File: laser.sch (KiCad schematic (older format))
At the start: 0 parts

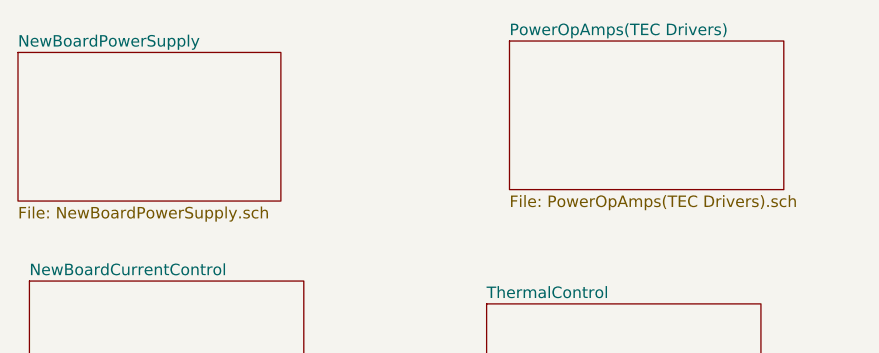
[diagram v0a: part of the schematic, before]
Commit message: added 4.2V port from pwr supply to pwr op amps sheet
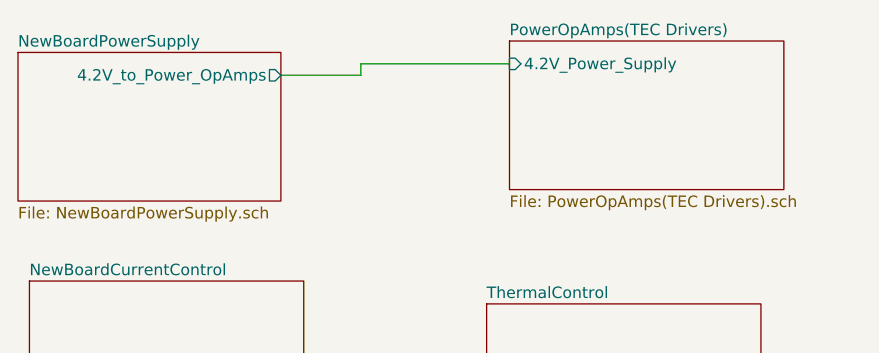
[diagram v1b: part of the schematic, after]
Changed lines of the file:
@@
 F0 "NewBoardPowerSupply" 50
 F1 "NewBoardPowerSupply.sch" 50
+F2 "4.2V_to_Power_OpAmps" O R 2850 1350 50
 $EndSheet
 $Sheet
@@
 F0 "PowerOpAmps(TEC Drivers)" 50
 F1 "PowerOpAmps(TEC Drivers).sch" 50
+F2 "4.2V_Power_Supply" I L 3850 1300 50
 $EndSheet
 $Sheet
@@
 F1 "ArduinoNano.sch" 50
 $EndSheet
+Wire Wire Line
+	2850 1350 3200 1350
+Wire Wire Line
+	3200 1350 3200 1300
+Wire Wire Line
+	3200 1300 3850 1300
 $EndSCHEMATC

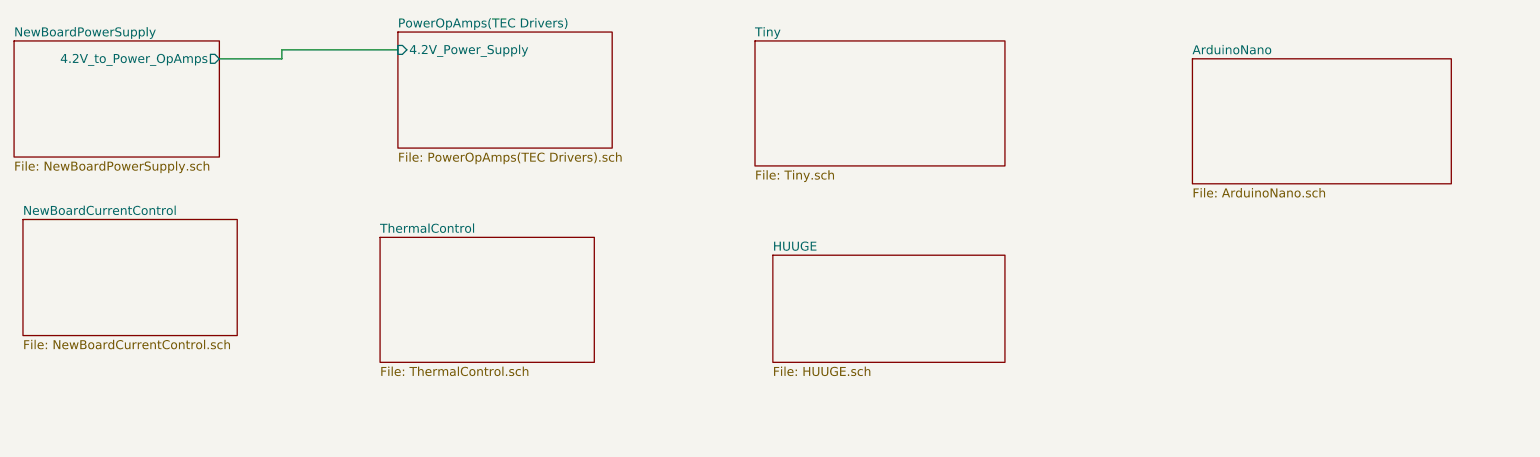
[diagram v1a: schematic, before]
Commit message: added 5v power source 'ports'
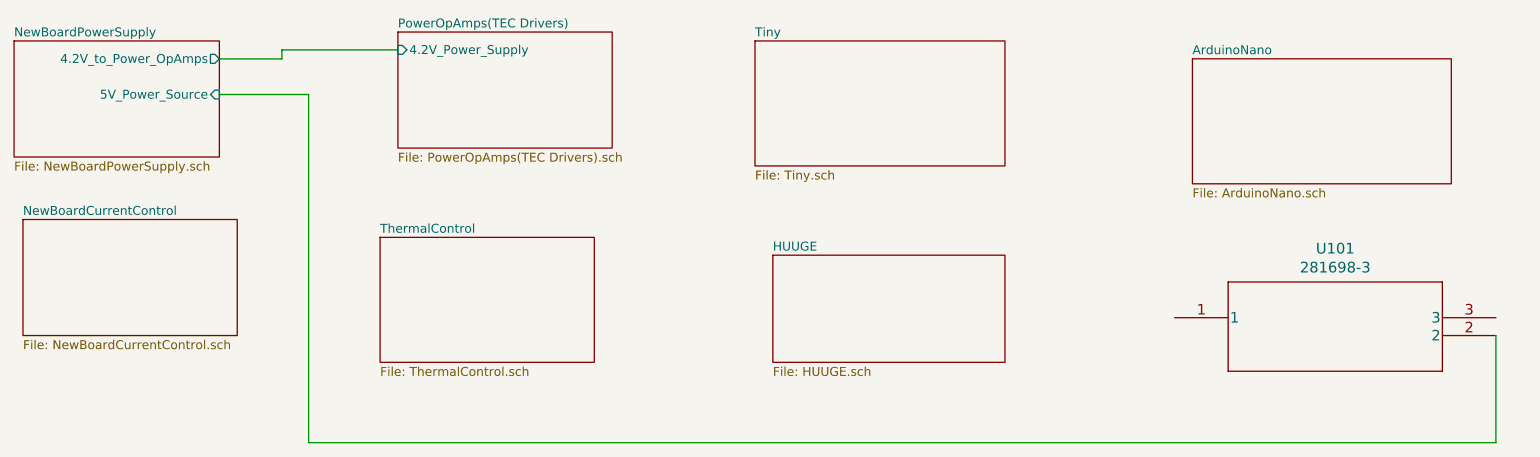
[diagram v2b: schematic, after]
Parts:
- added U101: 281698-3, footprint libraries:281698-3, symbol 3PinHeader:281698-3
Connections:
- new net NewBoardPowerSupply/5V_Power_Source: U101.2
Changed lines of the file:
@@
 F1 "NewBoardPowerSupply.sch" 50
 F2 "4.2V_to_Power_OpAmps" O R 2850 1350 50
+F3 "5V_Power_Source" I R 2850 1550 50
 $EndSheet
 $Sheet
@@
 Wire Wire Line
 	3200 1300 3850 1300
+$Comp
+L 3PinHeader:281698-3 U101
+U 1 1 60DB4391
+P 8200 2800
+F 0 "U101" H 9100 3187 60  0000 C CNN
+F 1 "281698-3" H 9100 3081 60  0000 C CNN
+F 2 "footprint libraries:281698-3" H 9100 3040 60  0001 C CNN
+F 3 "" H 8200 2800 60  0000 C CNN
+	1    8200 2800
+	1    0    0    -1
+$EndComp
+Wire Wire Line
+	2850 1550 3350 1550
+Wire Wire Line
+	3350 1550 3350 3500
+Wire Wire Line
+	3350 3500 10000 3500
+Wire Wire Line
+	10000 3500 10000 2900
 $EndSCHEMATC

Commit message: connect 5V label from nano on main
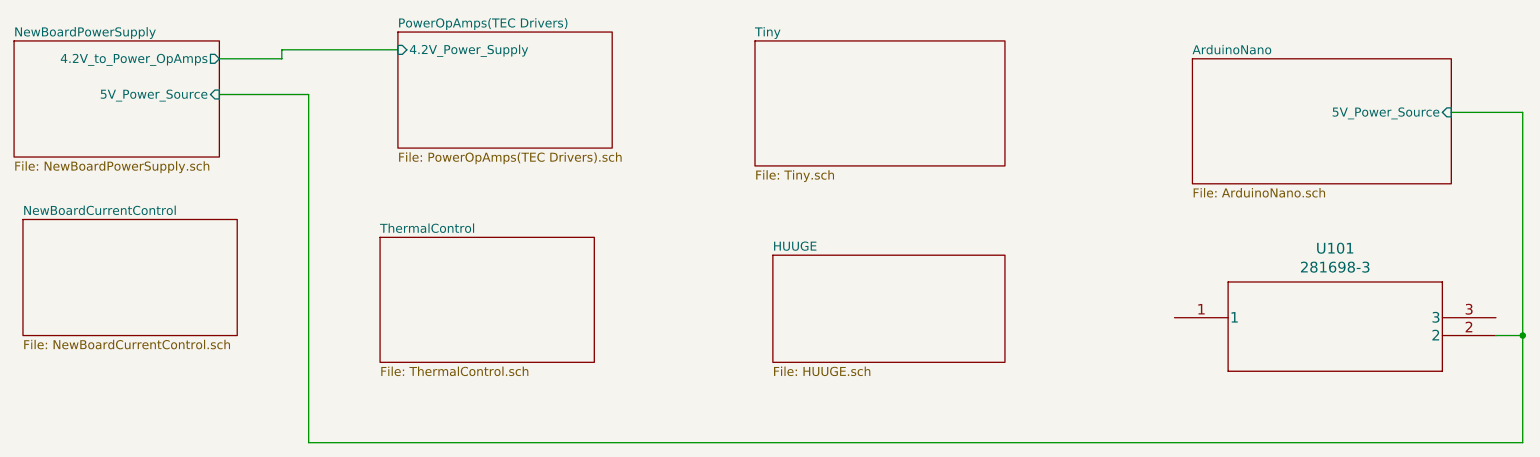
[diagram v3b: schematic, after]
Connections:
- net NewBoardPowerSupply/5V_Power_Source renamed ArduinoNano/5V_Power_Source
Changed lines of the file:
@@
 F0 "ArduinoNano" 50
 F1 "ArduinoNano.sch" 50
+F2 "5V_Power_Source" I R 9750 1650 50
 $EndSheet
 Wire Wire Line
@@
 	3350 1550 3350 3500
 Wire Wire Line
-	3350 3500 10000 3500
+	10150 3500 10150 2900
 Wire Wire Line
-	10000 3500 10000 2900
+	10150 2900 10000 2900
+Wire Wire Line
+	3350 3500 10150 3500
+Wire Wire Line
+	10150 2900 10150 1650
+Wire Wire Line
+	10150 1650 9750 1650
+Connection ~ 10150 2900
 $EndSCHEMATC

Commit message: ground
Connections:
- net GND: now reaches U101.1
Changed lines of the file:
@@
 	10150 1650 9750 1650
 Connection ~ 10150 2900
+$Comp
+L power:GND #PWR?
+U 1 1 60D4CF8B
+P 8200 2800
+F 0 "#PWR?" H 8200 2550 50  0001 C CNN
+F 1 "GND" V 8205 2672 50  0000 R CNN
+F 2 "" H 8200 2800 50  0001 C CNN
+F 3 "" H 8200 2800 50  0001 C CNN
+	1    8200 2800
+	0    1    1    0
+$EndComp
 $EndSCHEMATC

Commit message: add mod symbol
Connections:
- net NewBoardCurrentControl/MODULATION_SIGNAL: now reaches U101.3
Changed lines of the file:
@@
 F0 "NewBoardCurrentControl" 50
 F1 "NewBoardCurrentControl.sch" 50
+F2 "MODULATION_SIGNAL" I R 2950 2550 50
 $EndSheet
 $Sheet
@@
 	0    1    1    0
 $EndComp
+Wire Wire Line
+	2950 2550 3000 2550
+Wire Wire Line
+	3000 2550 3000 2150
+Wire Wire Line
+	3000 2150 10000 2150
+Wire Wire Line
+	10000 2150 10000 2800
 $EndSCHEMATC
